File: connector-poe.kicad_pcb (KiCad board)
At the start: 4 copper layers, 73.5 x 20 mm, 42 parts, among them J101 2x05_Horizontal, J102 NE8FAH, J103 JAE_DX07S016JA3, J104 2x05_Horizontal, J105 NE8FAH, J106 WAGO-2065, J107 WAGO-2065, J108 WAGO-2065, J109 WAGO-2065, Q201 BSC010N04LS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

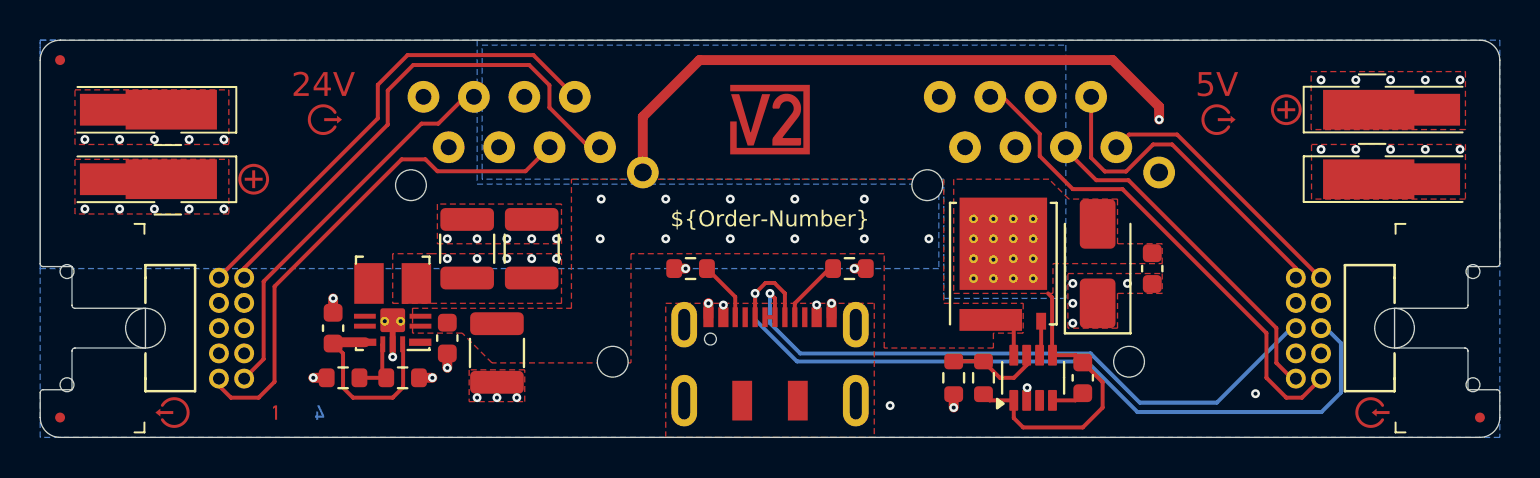
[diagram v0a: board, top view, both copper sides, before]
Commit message: Back-to-back Mosfet
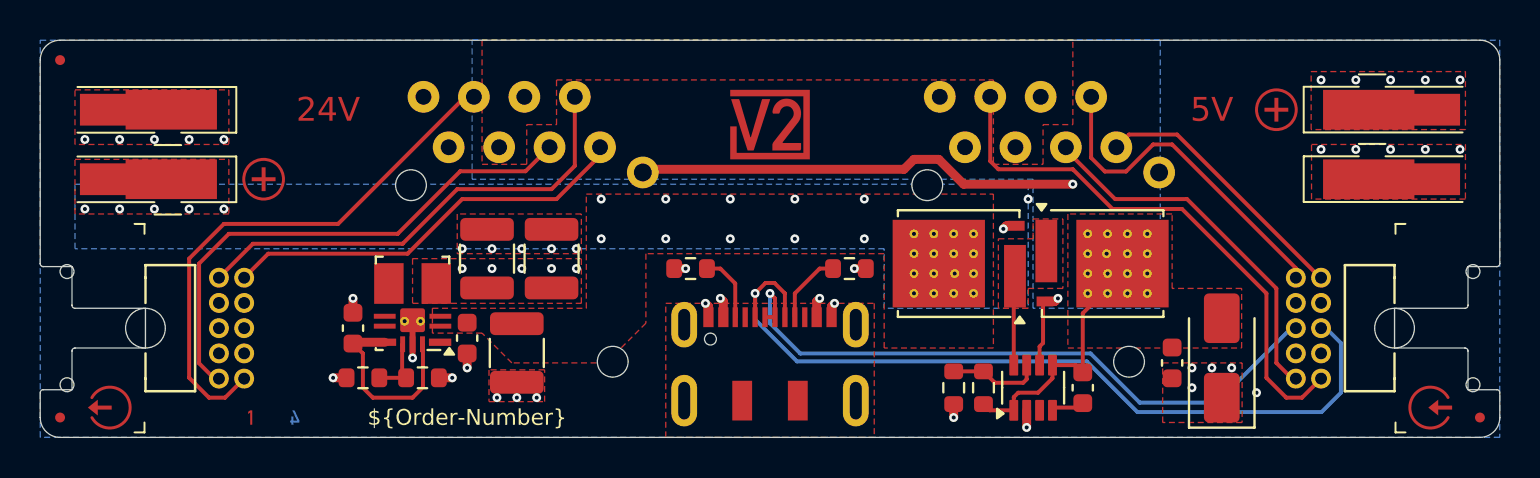
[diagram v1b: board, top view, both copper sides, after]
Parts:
- removed ICON110, ICON111: Arrow_Out, V2_Artwork:Arrow_Out
- added Q301: BSC010N04LS, V2_Package_TO_SOT_SMD:TDSON-8-FL, F.Cu at (163.2, 106.2)
- R202: value 4k7 -> 3k9
- moved INFO102 18.2 mm to (138.5, 114.0)
- moved TVS101 7.85 mm to (176.5, 111.0)
- moved Q201 5.00 mm to (170.5, 106.2), turned to 0 degrees
- moved C102 4.85 mm to (174.0, 111.2)
- moved ICON104 3.26 mm to (120.5, 113.5)
- moved ICON101 3.01 mm to (187.0, 113.5)
- moved ICON106 1.27 mm to (176.0, 98.5)
- moved ICON107 1.27 mm to (131.5, 98.5)
- moved INFO101 1.27 mm to (128.8, 114.0)
- moved C303 1.12 mm to (142.8, 106.0)
- moved C304 1.12 mm to (139.5, 106.0)
- moved C301 1.00 mm to (141.0, 110.8)
- moved C302 1.00 mm to (138.5, 110.0)
- moved C305 1.00 mm to (132.8, 109.5)
- moved R301 1.00 mm to (133.2, 112.0)
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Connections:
- C102 pad 1: /+24V-Input -> /+24V-Supply
- C201 pad 1: /+24V-Input -> /+24V-Supply
- C301 pad 1: /+24V-Supply -> +24V
- C302 pad 1: /+24V-Supply -> +24V
- J102 pad 4: /+24V-Input -> /+24V-Supply
- J102 pad 5: /+24V-Input -> /+24V-Supply
- J105 pad 4: /+24V-Input -> /+24V-Supply
- J105 pad 5: /+24V-Input -> /+24V-Supply
- J106 pad 1: /+24V-Supply -> +24V
- Q201 pad 1: /+24V-Supply -> /Polarity Protection/Source
- Q201 pad 5: /+24V-Input -> /+24V-Supply
- R201 pad 1: /+24V-Input -> /+24V-Supply
- TVS101 pad 2: /+24V-Input -> /+24V-Supply
- U201 pad 1: /+24V-Input -> /+24V-Supply
- U201 pad 5: /+24V-Input -> /+24V-Supply
- U201 pad 8: /+24V-Supply -> /Polarity Protection/Source
- U301 pad 2: /+24V-Supply -> +24V
- U301 pad 3: /+24V-Supply -> +24V
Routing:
- net /+24V-Input: track 15.2 -> 0.00 mm
- net /+24V-Supply: track 3.19 -> 12.8 mm, vias 16 -> 0
- net /Socket-TX-Z: track 19.7 -> 27.3 mm
- net /Polarity Protection/Gate: track 2.00 -> 9.39 mm, vias 0 -> 2
- net /RJ45-Shield: track 34.3 -> 27.2 mm
- net /Socket-RX-A: track 26.0 -> 21.4 mm
- net /Polarity Protection/Source: track 0.00 -> 4.00 mm
- net /Plug-RX-B: track 25.3 -> 27.7 mm
- net VBUS: track 5.94 -> 7.23 mm
- net /Plug-RX-A: track 17.5 -> 18.7 mm
- net /Socket-RX-B: track 24.4 -> 23.8 mm
- net /Socket-TX-Y: track 25.8 -> 26.4 mm
- net +24V: vias 0 -> 15
- added copper zone on B.Cu, net +24V
- added copper zone on F.Cu, net +24V
- added copper zone on In2.Cu, net +24V
- added copper zone on In2.Cu, net /+24V-Supply
- added copper zone on F.Cu, net /Polarity Protection/Source
- added copper zone on In2.Cu, net GND
- removed copper zone on B.Cu, net /+24V-Input
- removed copper zone on F.Cu, net /+24V-Input
- removed copper zone on In1.Cu, net /+24V-Input
- removed copper zone on In2.Cu, net /+24V-Input
